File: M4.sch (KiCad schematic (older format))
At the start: 179 parts

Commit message: almost finished schematic capture
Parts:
- removed R? (x2): 10, MyModules:SM0805-HAND, symbol R_US
- added C?: 10μ, MyModules:SM0805-HAND, symbol C_US
- added C?: 1μ, MyModules:SM0603-C-JRL, symbol C_US
- added C?: 22p, MyModules:SM0603-C-JRL, symbol C_US
- added L? (x3): 10μH, symbol INDUCTOR
- added R?: 47K, MyModules:SM0603-R-JRL, symbol R_US
- added R?: 91K, MyModules:SM0603-R-JRL, symbol R_US
- added U?: OPA171, TO_SOT_Packages_SMD:SOT-23-5, symbol TS321
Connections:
- net +12V: now also C?.1, L?.1, U?.5 (V+)
- net +3V3: now also C?.1, L?.1; no longer C?.1, U?.13 (VDDA)
- net -12V: now also L?.1, U?.2 (V-)
- net 12b_DAC: now also U?.3 (+); no longer P?.1 (P1), U?.3 (X)
- net GND: now also C?.2, C?.2, R?.2
- net at P?.1 (P1), P?.2 (P2): now also L?.2
- net at P?.10 (P10), P?.9 (P9): now also L?.2
- net DAC_AVDD: now reaches C?.1, C?.1, L?.2, U?.2 (AVDD)
- net at C?.1, U?.12 (X3): now also U?.12 (+); no longer U?.3 (+)
- net at C?.1, U?.15 (X2): now also U?.10 (+); no longer U?.3 (+)
- net at C?.1, R?.2: now also U?.8; no longer U?.1
- net at C?.2, R?.2: now also U?.9 (-); no longer U?.2 (-)
- net at C?.1, R?.2: now also U?.14; no longer U?.1
- net at C?.2, R?.2: now also U?.13 (-); no longer U?.2 (-)
- new net: C?.1, P?.1 (P1), R?.1, U?.1, U?.3 (X)
- new net: C?.1, L?.2, U?.13 (VDDA)
- new net: C?.2, R?.1, R?.2, U?.4 (-)
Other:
- note added: "03-2017"
- note added: "M4"
- note added: "MIDI PROCESSING UNIT"
- note added: "RATE POT"
- note added: "SLEW POT"
- note added: "SYSTEM 80"
- moved on the sheet: C?, D?, J?, L?, OC?, P?, R?, SW?, U?, U?A, U?B, U?C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

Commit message: updated panel svg for Inkscape 0.91, schematic annotated and ERC complete
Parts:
- added P7: CONN_01X01, MyModules:TEST_POINT_SMALL, symbol CONN_01X01
- L1, L2: renamed from L?; footprint (none) -> MyModules:SM0603-R-JRL
- U4: renamed from U?; footprint (none) -> Housings_SSOP:TSSOP-20_4.4x6.5mm_Pitch0.65mm
- Y1: renamed from Y?; footprint synth:403-XTAL-4-SMD -> synth:HC-49-SM
- gave numbers to parts that had none: 176
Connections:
- net PA2: now reaches U10.16 (ADC1_IN2/I2S_CKIN/TIM5_CH3/TIM9_CH1/USART2_TX/PA2)
- net PA2: now also P7.1 (P1)

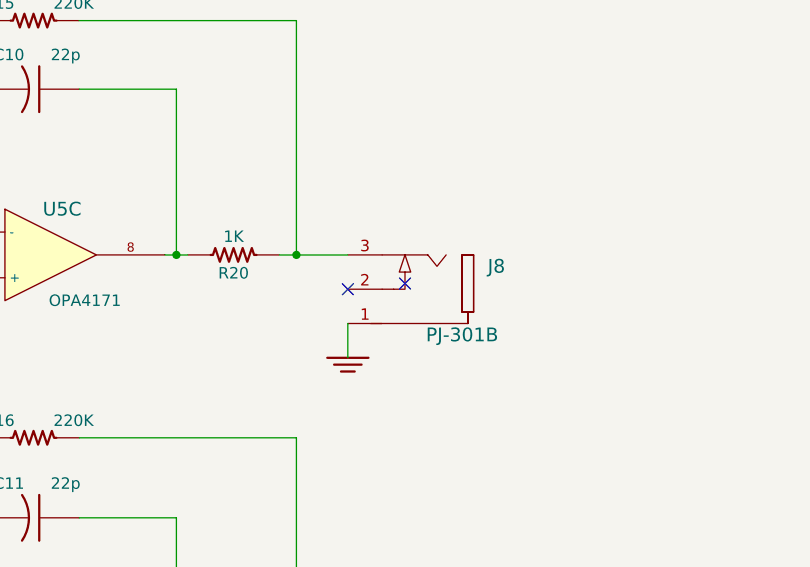
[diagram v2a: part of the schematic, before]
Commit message: placed pots/jacks/switches on PCB. not a lot of room left for ICs
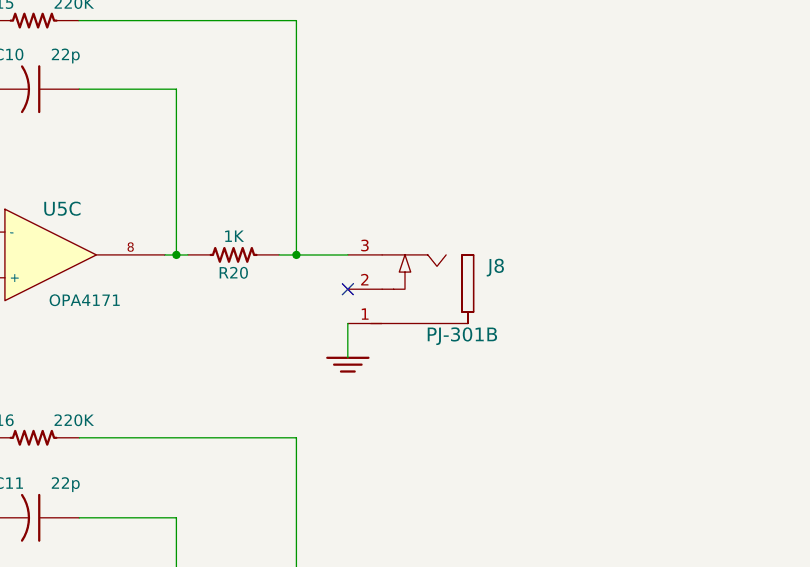
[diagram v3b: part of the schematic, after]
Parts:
- D1, D10, D11, D12, D13, D14, D15, D16, D17, D18, D19, D2, D20, D21, D3, D4, D5, D6, D7, D8, D9: footprint MyModules:LED-0805-JRL -> MyModules:1.8MM-LED-TLUG240
- D22: footprint (none) -> MyModules:SOD323-C1A2
- L3, L4: footprint (none) -> MyModules:SM0603-R-JRL
- P5: footprint (none) -> Pin_Headers:Pin_Header_Straight_1x06_Pitch2.54mm
- U10: footprint LQFP64 -> Housings_QFP:LQFP-64_10x10mm_Pitch0.5mm
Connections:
- no-connect marks 24 -> 23
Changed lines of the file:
@@
 F 0 "D20" V 9050 14850 50  0000 C CNN
 F 1 "LED" V 8975 14825 50  0000 C CNN
-F 2 "MyModules:LED-0805-JRL" H 9000 14700 60  0001 C CNN
+F 2 "MyModules:1.8MM-LED-TLUG240" H 9000 14700 60  0001 C CNN
 F 3 "" H 9000 14700 60  0000 C CNN
 	1    9000 14700
@@
 F 0 "D19" V 8750 14850 50  0000 C CNN
 F 1 "LED" V 8675 14825 50  0000 C CNN
-F 2 "MyModules:LED-0805-JRL" H 8700 14700 60  0001 C CNN
+F 2 "MyModules:1.8MM-LED-TLUG240" H 8700 14700 60  0001 C CNN
 F 3 "" H 8700 14700 60  0000 C CNN
 	1    8700 14700
@@
 F 0 "D18" V 8450 14850 50  0000 C CNN
 F 1 "LED" V 8375 14825 50  0000 C CNN
-F 2 "MyModules:LED-0805-JRL" H 8400 14700 60  0001 C CNN
+F 2 "MyModules:1.8MM-LED-TLUG240" H 8400 14700 60  0001 C CNN
 F 3 "" H 8400 14700 60  0000 C CNN
 	1    8400 14700
@@
 F 0 "D17" V 8150 14850 50  0000 C CNN
 F 1 "LED" V 8075 14825 50  0000 C CNN
-F 2 "MyModules:LED-0805-JRL" H 8100 14700 60  0001 C CNN
+F 2 "MyModules:1.8MM-LED-TLUG240" H 8100 14700 60  0001 C CNN
 F 3 "" H 8100 14700 60  0000 C CNN
 	1    8100 14700
@@
 Wire Wire Line
 	3550 7425 4625 7425
-NoConn ~ 6675 5750
 Wire Wire Line
 	3725 2125 3725 3675
@@
 F 0 "U10" H 13300 14450 50  0000 L BNN
 F 1 "STM32F410RBTx" H 18500 14450 50  0000 R BNN
-F 2 "LQFP64" H 18500 14400 50  0001 R TNN
+F 2 "Housings_QFP:LQFP-64_10x10mm_Pitch0.5mm" H 18500 14400 50  0001 R TNN
 F 3 "" H 15900 12525 50  0001 C CNN
 	1    15900 12525
@@
 F 0 "D22" H 11350 2875 50  0000 C CNN
 F 1 "1N4148" H 11350 2675 50  0000 C CNN
-F 2 "" H 11350 2775 60  0000 C CNN
+F 2 "MyModules:SOD323-C1A2" H 11350 2775 60  0001 C CNN
 F 3 "" H 11350 2775 60  0000 C CNN
 	1    11350 2775
@@
 F 0 "D1" H 6900 11025 50  0000 C CNN
 F 1 "LED" H 7125 11025 50  0000 C CNN
-F 2 "MyModules:LED-0805-JRL" H 7025 10900 60  0001 C CNN
+F 2 "MyModules:1.8MM-LED-TLUG240" H 7025 10900 60  0001 C CNN
 F 3 "" H 7025 10900 60  0000 C CNN
 	1    7025 10900
@@
 F 0 "D2" H 6900 11300 50  0000 C CNN
 F 1 "LED" H 7125 11300 50  0000 C CNN
-F 2 "MyModules:LED-0805-JRL" H 7025 11175 60  0001 C CNN
+F 2 "MyModules:1.8MM-LED-TLUG240" H 7025 11175 60  0001 C CNN
 F 3 "" H 7025 11175 60  0000 C CNN
 	1    7025 11175
@@
 F 0 "D3" H 6900 11575 50  0000 C CNN
 F 1 "LED" H 7125 11575 50  0000 C CNN
-F 2 "MyModules:LED-0805-JRL" H 7025 11450 60  0001 C CNN
+F 2 "MyModules:1.8MM-LED-TLUG240" H 7025 11450 60  0001 C CNN
 F 3 "" H 7025 11450 60  0000 C CNN
 	1    7025 11450
@@
 F 0 "D4" H 6900 11850 50  0000 C CNN
 F 1 "LED" H 7125 11850 50  0000 C CNN
-F 2 "MyModules:LED-0805-JRL" H 7025 11725 60  0001 C CNN
+F 2 "MyModules:1.8MM-LED-TLUG240" H 7025 11725 60  0001 C CNN
 F 3 "" H 7025 11725 60  0000 C CNN
 	1    7025 11725
@@
 F 0 "D5" H 6900 12150 50  0000 C CNN
 F 1 "LED" H 7125 12150 50  0000 C CNN
-F 2 "MyModules:LED-0805-JRL" H 7025 12025 60  0001 C CNN
+F 2 "MyModules:1.8MM-LED-TLUG240" H 7025 12025 60  0001 C CNN
 F 3 "" H 7025 12025 60  0000 C CNN
 	1    7025 12025
@@
 F 0 "D6" H 6900 12425 50  0000 C CNN
 F 1 "LED" H 7125 12425 50  0000 C CNN
-F 2 "MyModules:LED-0805-JRL" H 7025 12300 60  0001 C CNN
+F 2 "MyModules:1.8MM-LED-TLUG240" H 7025 12300 60  0001 C CNN
 F 3 "" H 7025 12300 60  0000 C CNN
 	1    7025 12300
@@
 F 0 "D7" H 6900 12700 50  0000 C CNN
 F 1 "LED" H 7125 12700 50  0000 C CNN
-F 2 "MyModules:LED-0805-JRL" H 7025 12575 60  0001 C CNN
+F 2 "MyModules:1.8MM-LED-TLUG240" H 7025 12575 60  0001 C CNN
 F 3 "" H 7025 12575 60  0000 C CNN
 	1    7025 12575
@@
 F 0 "D8" H 6900 12975 50  0000 C CNN
 F 1 "LED" H 7125 12975 50  0000 C CNN
-F 2 "MyModules:LED-0805-JRL" H 7025 12850 60  0001 C CNN
+F 2 "MyModules:1.8MM-LED-TLUG240" H 7025 12850 60  0001 C CNN
 F 3 "" H 7025 12850 60  0000 C CNN
 	1    7025 12850
@@
 F 0 "D9" H 6900 13275 50  0000 C CNN
 F 1 "LED" H 7125 13275 50  0000 C CNN
-F 2 "MyModules:LED-0805-JRL" H 7025 13150 60  0001 C CNN
+F 2 "MyModules:1.8MM-LED-TLUG240" H 7025 13150 60  0001 C CNN
 F 3 "" H 7025 13150 60  0000 C CNN
 	1    7025 13150
@@
 F 0 "D10" H 6900 13550 50  0000 C CNN
 F 1 "LED" H 7125 13550 50  0000 C CNN
-F 2 "MyModules:LED-0805-JRL" H 7025 13425 60  0001 C CNN
+F 2 "MyModules:1.8MM-LED-TLUG240" H 7025 13425 60  0001 C CNN
 F 3 "" H 7025 13425 60  0000 C CNN
 	1    7025 13425
@@
 F 0 "D11" H 6900 13825 50  0000 C CNN
 F 1 "LED" H 7125 13825 50  0000 C CNN
-F 2 "MyModules:LED-0805-JRL" H 7025 13700 60  0001 C CNN
+F 2 "MyModules:1.8MM-LED-TLUG240" H 7025 13700 60  0001 C CNN
 F 3 "" H 7025 13700 60  0000 C CNN
 	1    7025 13700
@@
 F 0 "D12" H 6900 14100 50  0000 C CNN
 F 1 "LED" H 7125 14100 50  0000 C CNN
-F 2 "MyModules:LED-0805-JRL" H 7025 13975 60  0001 C CNN
+F 2 "MyModules:1.8MM-LED-TLUG240" H 7025 13975 60  0001 C CNN
 F 3 "" H 7025 13975 60  0000 C CNN
 	1    7025 13975
@@
 F 0 "D13" H 6900 14400 50  0000 C CNN
 F 1 "LED" H 7125 14400 50  0000 C CNN
-F 2 "MyModules:LED-0805-JRL" H 7025 14275 60  0001 C CNN
+F 2 "MyModules:1.8MM-LED-TLUG240" H 7025 14275 60  0001 C CNN
 F 3 "" H 7025 14275 60  0000 C CNN
 	1    7025 14275
@@
 F 0 "D14" H 6900 14675 50  0000 C CNN
 F 1 "LED" H 7125 14675 50  0000 C CNN
-F 2 "MyModules:LED-0805-JRL" H 7025 14550 60  0001 C CNN
+F 2 "MyModules:1.8MM-LED-TLUG240" H 7025 14550 60  0001 C CNN
 F 3 "" H 7025 14550 60  0000 C CNN
 	1    7025 14550
@@
 F 0 "D15" H 6900 14950 50  0000 C CNN
 F 1 "LED" H 7125 14950 50  0000 C CNN
-F 2 "MyModules:LED-0805-JRL" H 7025 14825 60  0001 C CNN
+F 2 "MyModules:1.8MM-LED-TLUG240" H 7025 14825 60  0001 C CNN
 F 3 "" H 7025 14825 60  0000 C CNN
 	1    7025 14825
@@
 F 0 "D16" H 6900 15225 50  0000 C CNN
 F 1 "LED" H 7125 15225 50  0000 C CNN
-F 2 "MyModules:LED-0805-JRL" H 7025 15100 60  0001 C CNN
+F 2 "MyModules:1.8MM-LED-TLUG240" H 7025 15100 60  0001 C CNN
 F 3 "" H 7025 15100 60  0000 C CNN
 	1    7025 15100
@@
 F 0 "P5" H 17825 9675 50  0000 C CNN
 F 1 "CONN_01X06" V 17925 9325 50  0000 C CNN
-F 2 "" H 17825 9325 60  0000 C CNN
+F 2 "Pin_Headers:Pin_Header_Straight_1x06_Pitch2.54mm" H 17825 9325 60  0001 C CNN
 F 3 "" H 17825 9325 60  0000 C CNN
 	1    17825 9325
@@
 F 0 "D21" V 9350 14850 50  0000 C CNN
 F 1 "LED" V 9275 14825 50  0000 C CNN
-F 2 "MyModules:LED-0805-JRL" H 9300 14700 60  0001 C CNN
+F 2 "MyModules:1.8MM-LED-TLUG240" H 9300 14700 60  0001 C CNN
 F 3 "" H 9300 14700 60  0000 C CNN
 	1    9300 14700
@@
 F 0 "L3" V 19475 1375 50  0000 C CNN
 F 1 "10μH" V 19400 1325 50  0000 C CNN
-F 2 "" H 19300 1325 60  0000 C CNN
+F 2 "MyModules:SM0603-R-JRL" H 19300 1325 60  0001 C CNN
 F 3 "" H 19300 1325 60  0000 C CNN
 	1    19300 1325
@@
 F 0 "L4" V 19500 2275 50  0000 C CNN
 F 1 "10μH" V 19425 2225 50  0000 C CNN
-F 2 "" H 19325 2225 60  0000 C CNN
+F 2 "MyModules:SM0603-R-JRL" H 19325 2225 60  0001 C CNN
 F 3 "" H 19325 2225 60  0000 C CNN
 	1    19325 2225

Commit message: routing.
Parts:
- Y1: footprint synth:HC-49-SM -> synth:403-XTAL-4-SMD
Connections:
- net DAC_CH1: now reaches U5.10 (+)
- net DAC_CH1: now also U3.14 (OUT1); no longer U3.11 (OUT2)
- net DAC_CH0: now reaches U5.5 (+)
- net DAC_CH0: now also U3.3 (OUT0); no longer U3.14 (OUT1)
- net DAC_CH3: now reaches U5.3 (+)
- net DAC_CH3: now also U3.6 (OUT3); no longer U3.3 (OUT0)
- net DAC_CH2: now reaches U5.12 (+)
- net DAC_CH2: now also U3.11 (OUT2); no longer U3.6 (OUT3)
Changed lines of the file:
@@
 	5250 1175 5675 1175
 Wire Wire Line
-	2750 3975 3650 3975
-Wire Wire Line
-	2750 4125 3550 4125
-Wire Wire Line
 	9725 3950 10300 3950
 Wire Wire Line
@@
 	5275 875  6200 875
 Connection ~ 6200 2025
-Wire Wire Line
-	3550 4125 3550 7425
-Wire Wire Line
-	3725 2125 4625 2125
 $Comp
 L CONN_01X01 P1
@@
 Connection ~ 6200 5625
 Connection ~ 6200 7325
-Wire Wire Line
-	3650 5725 4625 5725
-Wire Wire Line
-	3550 7425 4625 7425
-Wire Wire Line
-	3725 2125 3725 3675
-Wire Wire Line
-	3725 3675 2750 3675
-Wire Wire Line
-	3650 3975 3650 5725
 $Comp
 L TL074- U5
@@
 	1    0    0    -1
 $EndComp
-Wire Wire Line
-	2750 3825 3725 3825
-Wire Wire Line
-	3725 3825 3725 4000
-Wire Wire Line
-	3725 4000 4625 4000
 $Comp
 L TL074- U5
@@
 F 0 "Y1" V 12025 12500 50  0000 C CNN
 F 1 "8MHz" V 12150 12700 50  0000 C CNN
-F 2 "synth:HC-49-SM" H 12150 12375 60  0001 C CNN
+F 2 "synth:403-XTAL-4-SMD" H 12150 12375 60  0001 C CNN
 F 3 "" H 12150 12375 60  0000 C CNN
 	1    12150 12375
@@
 	16525 9725 16525 9800
 Connection ~ 16525 9800
+Text Label 2750 3675 0    60   ~ 0
+DAC_CH0
+Text Label 2750 3825 0    60   ~ 0
+DAC_CH1
+Text Label 2750 3975 0    60   ~ 0
+DAC_CH2
+Text Label 2750 4125 0    60   ~ 0
+DAC_CH3
+Text Label 4625 4000 2    60   ~ 0
+DAC_CH0
+Text Label 4625 5725 2    60   ~ 0
+DAC_CH1
+Text Label 4625 7425 2    60   ~ 0
+DAC_CH2
+Text Label 4625 2125 2    60   ~ 0
+DAC_CH3
 $EndSCHEMATC
